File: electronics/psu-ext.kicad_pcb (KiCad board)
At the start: 4 copper layers, 100 x 50 mm, 115 parts, among them J1 TYPE-C-31-M-12, J2 Conn_01x03, J4 Conn_02x02_Odd_Even, K1 HF49FD_005-1H12T, Q1 MMBT2222A, SW1 SW_Push, SW2 SW_Push, U1 USBLC6-2SC6, U2 AP22818AKEWT, U3 LD1117S33, U4 LD1117S33, U5 ESP32-S3-WROOM-1, U6 ISO1540, U7 ADS1115IDGS, U8 INA240A2D, U9 W25Q16JVSS, Y1 FC-135_32.7680KA-A0

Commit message: Add current-sense amplifier offset and fix first-boot download mode
Improve measurement accuracy near zero and enable bidirectional current sensing by adding the current-sense amplifier offset.

Resolve the download-mode issue encountered on first boot.

Signed-off-by: Maxim Pavlov <max.eelabs@gmail.com>
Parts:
- added C24: 100nF, Capacitor_SMD:C_0805_2012Metric, B.Cu at (154.7, 106.6)
- added R27: 22k, Resistor_SMD:R_0805_2012Metric, B.Cu at (157.1, 102.5)
- added R28: 2k, Resistor_SMD:R_0805_2012Metric, B.Cu at (159.1, 102.5)
- added U10: LM321, Package_TO_SOT_SMD:SOT-23-5, B.Cu at (158.0, 106.6)
- moved TP7 0.90 mm to (153.0, 122.1)
- moved TP6 0.85 mm to (157.0, 102.0), turned to 45 degrees
- renumbered C24 to C25, C25 to C26, C26 to C27, C27 to C28, C28 to C29, C29 to C30, C30 to C31, R27 to R29, R28 to R30, R29 to R31, R30 to R32, R31 to R33, R32 to R34, R33 to R35, R34 to R36, R35 to R37, R36 to R38, R37 to R39, R38 to R40, R39 to R41, R40 to R42, R41 to R43, R42 to R44
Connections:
- U8 pad 7: GNDS -> Net-(U10--)
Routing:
- net Net-(U10--): track 0.00 -> 9.25 mm, vias 0 -> 1
- net V3.3-F: track 31.6 -> 36.7 mm
- net Net-(U10-+): track 0.00 -> 4.22 mm
- net GNDS: track 9.90 -> 12.0 mm, vias 27 -> 33
- net /FrontEnd/ALRT: track 9.29 -> 8.77 mm

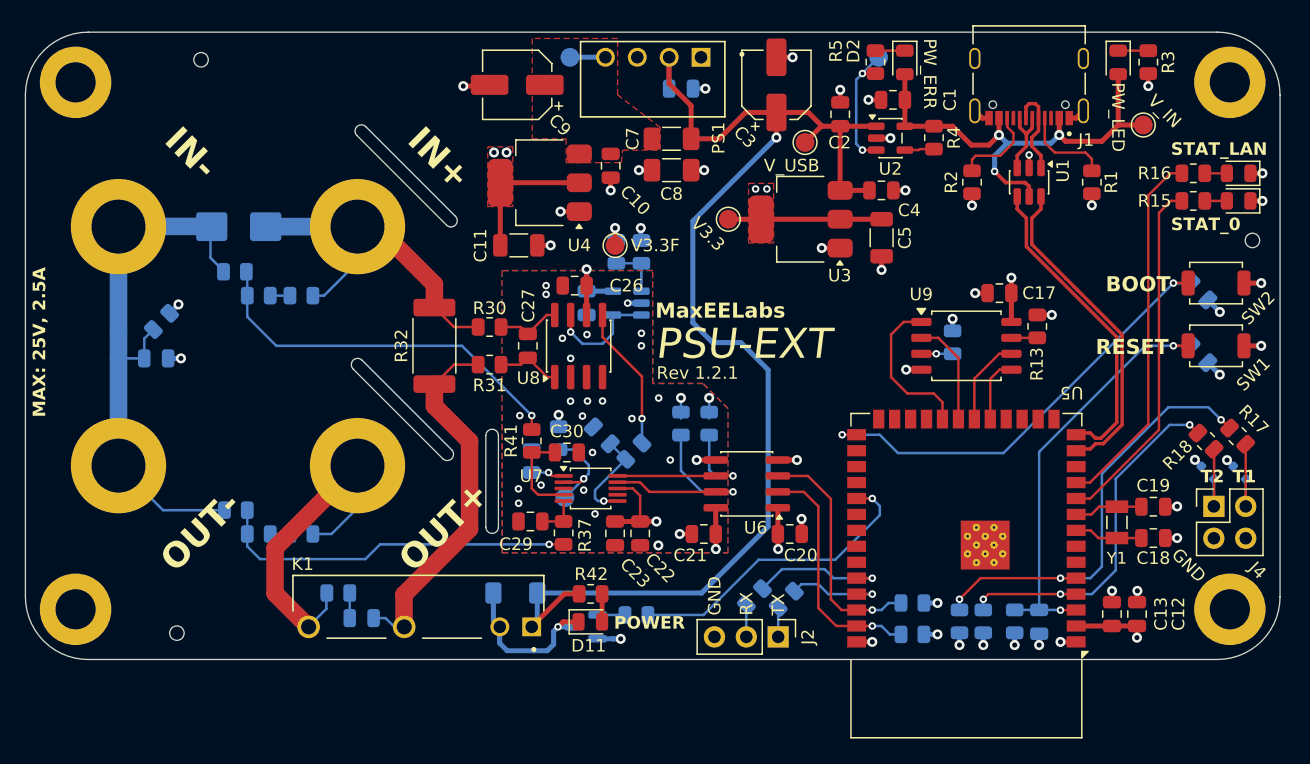
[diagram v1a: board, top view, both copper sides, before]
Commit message: Added input buffernig and negative rail for near-zero measurments
Added I2C_NUM_1 on IO6 (SDA) and IO7 (SCL).

Signed-off-by: Maxim Pavlov <max.eelabs@gmail.com>
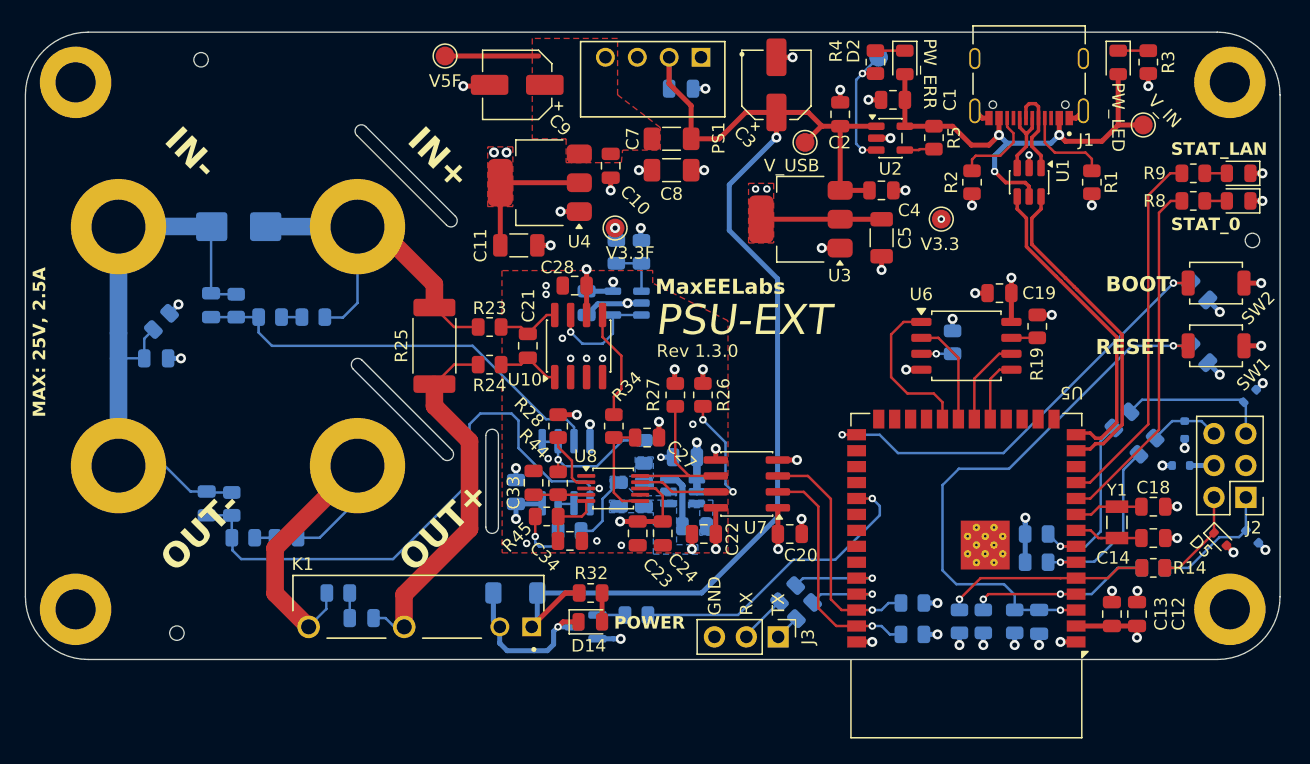
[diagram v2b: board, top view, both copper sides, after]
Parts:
- removed the C25 at (155.9, 117.1)
- removed the C29 at (150.3, 124.0)
- removed J4: Conn_02x02_Odd_Even, Connector_PinHeader_2.54mm:PinHeader_2x02_P2.54mm_Vertical
- removed the R25 at (152.5, 117.4)
- removed the R26 at (150.4, 119.2)
- removed the R29 at (158.5, 118.4)
- removed the R35 at (128.6, 125.0)
- removed TP7: ALRT, TestPoint:TestPoint_Pad_D1.5mm
- added C27: 100nF, Capacitor_SMD:C_0805_2012Metric, F.Cu at (159.6, 117.3)
- added C31: 10nF, Capacitor_SMD:C_0805_2012Metric, B.Cu at (124.8, 106.8)
- added C32: 100nF, Capacitor_SMD:C_0805_2012Metric, B.Cu at (149.1, 121.7)
- added C33: 100nF, Capacitor_SMD:C_0805_2012Metric, F.Cu at (150.5, 120.9)
- added C34: 100nF, Capacitor_SMD:C_0805_2012Metric, F.Cu at (153.4, 125.5)
- added C35: 22uF, Capacitor_SMD:C_0805_2012Metric, B.Cu at (162.6, 118.9)
- added C36: 10uF, Capacitor_SMD:C_0805_2012Metric, B.Cu at (163.3, 124.4)
- added C37: 22uF, Capacitor_SMD:C_0805_2012Metric, B.Cu at (157.3, 121.8)
- added C38: 22uF, Capacitor_SMD:C_0805_2012Metric, B.Cu at (159.3, 121.8)
- added D7: ESD5Zxx, Diode_SMD:D_SOD-523, B.Cu at (207.6, 114.0)
- added D8: ESD5Zxx, Diode_SMD:D_SOD-523, B.Cu at (202.4, 116.7)
- added D9: ESD5Zxx, Diode_SMD:D_SOD-523, B.Cu at (202.1, 119.5)
- added J2: Conn_02x03_Odd_Even, Connector_PinHeader_2.54mm:PinHeader_2x03_P2.54mm_Vertical, F.Cu at (207.3, 122.1)
- added R12: 4.7k, Resistor_SMD:R_0805_2012Metric, B.Cu at (190.6, 127.2)
- added R13: 4.7k, Resistor_SMD:R_0805_2012Metric, B.Cu at (190.6, 125.0)
- added R16: 22R, Resistor_SMD:R_0805_2012Metric, B.Cu at (197.4, 115.9)
- added R17: 22R, Resistor_SMD:R_0805_2012Metric, B.Cu at (199.4, 118.0)
- added R28: 10k, Resistor_SMD:R_0805_2012Metric, F.Cu at (152.5, 116.4)
- added R42: 20k, Resistor_SMD:R_0805_2012Metric, B.Cu at (159.3, 118.5)
- added R43: 20k, Resistor_SMD:R_0805_2012Metric, B.Cu at (153.4, 124.8)
- added R44: 1k, Resistor_SMD:R_0805_2012Metric, F.Cu at (152.5, 121.0)
- added R45: 1k, Resistor_SMD:R_0805_2012Metric, F.Cu at (151.6, 123.6)
- added U11: TSZ122IYDT, Package_SO:SOIC-8_3.9x4.9mm_P1.27mm, B.Cu at (153.1, 120.1)
- added U12: LM2664M6, Package_TO_SOT_SMD:SOT-23-6, B.Cu at (162.4, 121.6)
- C30: value 1nF -> 10nF; moved to B.Cu
- D5, TP5: moved to F.Cu
- R15: renamed from R18; moved to B.Cu
- R26: renamed from R23; moved to F.Cu
- R27: renamed from R24; moved to F.Cu
- R34: value 160k -> 1.5k; moved to F.Cu
- R36: value 20k -> 160k
- R37: value 1k -> 160k; moved to B.Cu
- R41: value 1k -> 20k; moved to B.Cu
- moved C30 29.0 mm to (124.5, 122.6), turned to 90 degrees
- moved R34 26.3 mm to (156.9, 116.4), turned to 90 degrees
- moved R37 26.3 mm to (132.9, 107.7), turned to 180 degrees
- moved R41 25.9 mm to (126.8, 106.8), turned to -90 degrees
- moved R38 19.8 mm to (127.4, 125.3)
- moved R40 18.5 mm to (126.5, 122.6), turned to -90 degrees
- moved TP4 17.0 mm to (183.0, 99.9)
- moved R14 12.5 mm to (199.9, 127.7), turned to 0 degrees
- moved R15 10.9 mm to (199.9, 127.7), turned to 0 degrees
- moved TP5 9.95 mm to (143.4, 86.9), turned to 180 degrees
- moved D6 6.20 mm to (207.8, 125.2), turned to -45 degrees
- moved D5 5.52 mm to (205.2, 125.4), turned to -45 degrees
- moved R36 4.60 mm to (130.8, 125.3), turned to 180 degrees
- moved R27 3.54 mm to (161.8, 113.9)
- moved R26 2.88 mm to (164.0, 113.9)
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- renumbered C18 to C14, C14 to C15, C15 to C16, C16 to C17, C19 to C18, C17 to C19, C27 to C21, C21 to C22, C22 to C24, C28 to C25, C24 to C26, C26 to C28, C31 to C29, D10 to D13, D11 to D14, D12 to D15, H5 to H1, H4 to H10, H3 to H11, H6 to H2, H7 to H3, H8 to H4, H9 to H5, H10 to H6, H11 to H7, H2 to H8, H1 to H9, J2 to J3, R8 to R10, R9 to R11, R17 to R14, R10 to R18, R13 to R19, R14 to R20, R11 to R21, R12 to R22, R30 to R23, R31 to R24, R32 to R25, R33 to R29, R27 to R30, R28 to R31, R42 to R32, R43 to R33, R44 to R35, R5 to R4, R4 to R5, R15 to R8, R16 to R9, U8 to U10, U9 to U6, U6 to U7, U7 to U8, U10 to U9
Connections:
- net /FrontEnd/SCLS renamed /FrontEnd ADC/SCLS
- net /FrontEnd/SDAS renamed /FrontEnd ADC/SDAS
- net /FrontEnd/SENSE_N renamed /FrontEnd ADC/SENSE_N
- net /FrontEnd/SENSE_P renamed /FrontEnd ADC/SENSE_P
- net /FrontEnd/SNT_N renamed /FrontEnd ADC/SNT_N
- C25 pad 1: /FrontEnd/PGND -> PGND
- C30 pad 1: /FrontEnd/AIN0 -> Net-(U11B-+)
- C30 pad 2: GNDS -> PGND
- D13 pad 1: /FrontEnd/PSU_P -> PSU_P
- D13 pad 2: /FrontEnd/PGND -> PGND
- H10 pad 1: /FrontEnd/PGND -> PGND
- H11 pad 1: /FrontEnd/PGND -> PGND
- H8 pad 1: /FrontEnd/PSU_P -> PSU_P
- H9 pad 1: /FrontEnd/LOAD_P -> LOAD_P
- K1 pad 4: /FrontEnd/LOAD_P -> LOAD_P
- R23 pad 2: /FrontEnd/PSU_P -> PSU_P
- R25 pad 2: /FrontEnd/PSU_P -> PSU_P
- R29 pad 1: /FrontEnd/PGND -> PGND
- R34 pad 1: /FrontEnd/LOAD_P -> /FrontEnd ADC/AIN2
- R35 pad 1: /FrontEnd/LOAD_P -> LOAD_P
- R36 pad 1: /FrontEnd/PGND -> LOAD_P
- R36 pad 2: Net-(R35-Pad2) -> Net-(R36-Pad2)
- R37 pad 1: /FrontEnd/AIN1 -> PSU_P
- R37 pad 2: Net-(R35-Pad2) -> Net-(R37-Pad2)
- R38 pad 1: /FrontEnd/PSU_P -> Net-(R36-Pad2)
- R38 pad 2: Net-(R38-Pad2) -> Net-(U11B-+)
- R39 pad 1: Net-(R38-Pad2) -> Net-(R37-Pad2)
- R39 pad 2: Net-(R39-Pad2) -> Net-(U11A-+)
- R40 pad 1: /FrontEnd/PGND -> PGND
- R40 pad 2: Net-(R39-Pad2) -> Net-(U11B-+)
- R41 pad 1: /FrontEnd/AIN0 -> PGND
- R41 pad 2: Net-(R39-Pad2) -> Net-(U11A-+)
- U10 pad 5: Net-(R29-Pad2) -> Net-(R34-Pad2)
- U5 pad 6: unconnected-(U5-IO6-Pad6) -> /ESP32/SDA1
- U5 pad 7: unconnected-(U5-IO7-Pad7) -> /ESP32/SCL1
- U8 pad 1: Net-(U7-ADDR) -> GNDS
- U8 pad 2: /FrontEnd/ALRT -> Net-(U8-ALERT/RDY)
- U8 pad 4: /FrontEnd/AIN0 -> AIN0
- U8 pad 5: /FrontEnd/AIN1 -> AIN1
- U8 pad 6: /FrontEnd/AIN2 -> /FrontEnd ADC/AIN2
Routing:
- net PGND: track 0.00 -> 48.9 mm
- net Net-(U11B-+): track 0.00 -> 46.1 mm
- net /FrontEnd/PGND: track 45.5 -> 0.00 mm
- net LOAD_P: track 0.00 -> 35.7 mm
- net Net-(U11A-+): track 0.00 -> 34.4 mm
- net /FrontEnd/LOAD_P: track 31.3 -> 0.00 mm
- net Net-(R39-Pad2): track 30.6 -> 0.00 mm, vias 1 -> 0
- net PSU_P: track 0.00 -> 30.1 mm
- net Net-(R35-Pad2): track 29.0 -> 0.00 mm, vias 1 -> 0
- net /FrontEnd/PSU_P: track 29.0 -> 0.00 mm
- net /ESP32/TRG2: track 35.1 -> 16.4 mm, vias 3 -> 1
- net /ESP32/SDA1: track 0.00 -> 15.1 mm, vias 0 -> 1
- net /ESP32/SCL1: track 0.00 -> 15.1 mm, vias 0 -> 1
- net /ESP32/TRG1: track 29.7 -> 15.9 mm, vias 3 -> 2
- net Net-(D7-K): track 0.00 -> 12.1 mm
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- added copper zone on B.Cu, net -3V3
- added copper zone on B.Cu, net Net-(U12-CAP+)
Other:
- board text added: "CERN-OHL-S v2 Source: github.com/PSU-Ext-Org"
- board text removed: "CERN-OHL-S v2 Source: github.com/PSU-Ext-Org/psu-ext"
- board text removed: "T1"
- board text removed: "T2"

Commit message: Added IO3 pullup and negative 3V3 rail testpoint, few other PCB layput improvements.
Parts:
- added R14: 10k, Resistor_SMD:R_0805_2012Metric, F.Cu at (193.9, 112.4)
- added TP7: -3V3, TestPoint:TestPoint_Pad_D1.5mm, F.Cu at (160.0, 112.9)
- C7, C8: value 330p 1kV -> 330p
- D6, D7, D8, D9: value ESD5Zxx -> ESD5Z3.3T1G
- R21: renamed from R20; moved to F.Cu
- R3: value 1k -> 2.2k
- moved R21 4.41 mm to (182.1, 105.7), turned to 0 degrees
- moved R43 2.00 mm to (157.3, 118.5)
- moved R27 1.31 mm to (165.3, 113.8)
- moved R28 1.31 mm to (163.1, 113.8)
- moved R35 1.14 mm to (156.9, 117.5)
- moved C27 0.68 mm to (158.9, 117.5), turned to 90 degrees
- moved R20 0.25 mm to (190.9, 108.4)
- renumbered R14 to R15, R15 to R16, R16 to R17, R17 to R18, R18 to R19, R19 to R20, R21 to R22, R22 to R23, R23 to R24, R24 to R25, R25 to R26, R26 to R27, R27 to R28, R28 to R29, R29 to R30, R30 to R31, R31 to R32, R32 to R33, R33 to R34, R34 to R35, R35 to R36, R36 to R37, R37 to R38, R38 to R39, R39 to R40, R40 to R41, R41 to R42, R42 to R43, R43 to R44, R44 to R45, R45 to R46
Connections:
- U5 pad 15: unconnected-(U5-IO3-Pad15) -> Net-(U5-IO3)
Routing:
- net -3V3: track 5.63 -> 14.3 mm, vias 0 -> 1
- net Net-(U6-~{WP}/IO_{2}): track 2.52 -> 8.68 mm, vias 1 -> 2
- net Net-(U5-IO3): track 0.00 -> 3.91 mm
- net Net-(U11A--): track 11.6 -> 10.4 mm
- net /FrontEnd ADC/AIN2: track 8.47 -> 7.63 mm
- net V3.3: track 35.0 -> 35.7 mm, vias 14 -> 15
- net /FrontEnd ADC/SCLS: track 12.0 -> 12.7 mm

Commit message: Fixex for proect before PCBA. TODO. BOM, CPL, EXPORT
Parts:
- D5: value ESD5Zxx -> ESD5Z3.3T1G
- R3: value 2.2k -> 2k
- R31: value 22k -> 20k
- R4: value 1k -> 2k

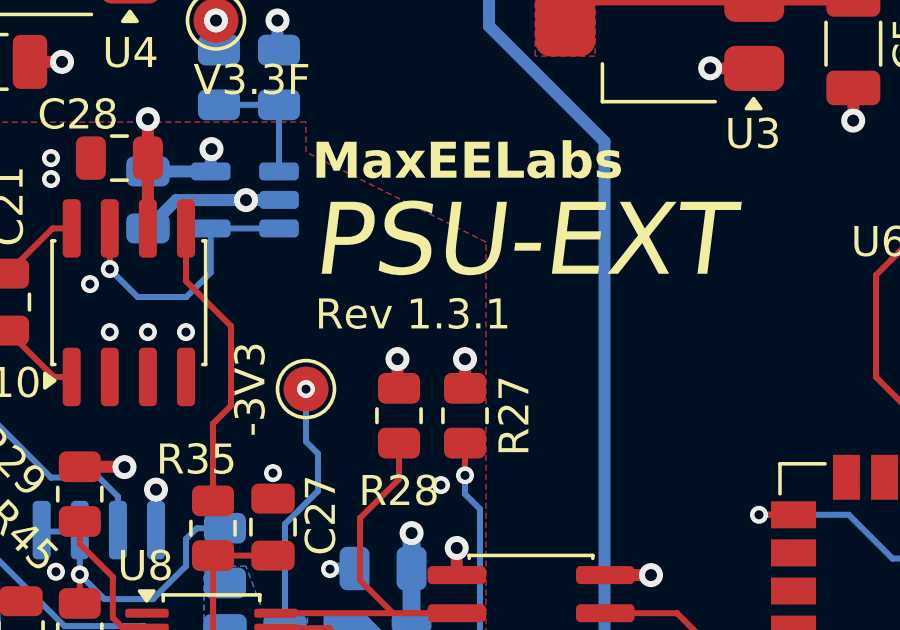
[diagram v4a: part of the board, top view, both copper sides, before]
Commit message: Replaced USB power switch and refreshed manufacturing exports (#5)
Replaced USB power switch U2 with AP2151DWG-7 (0.8 A). Updated schematic and PCB revision metadata and regenerated the BOM, CPL, schematic PDF, and Gerbers.

Updated CHANGES.txt with the design changes and removed completed export TODOs.

Signed-off-by: Maxim Pavlov <max.eelabs@gmail.com>
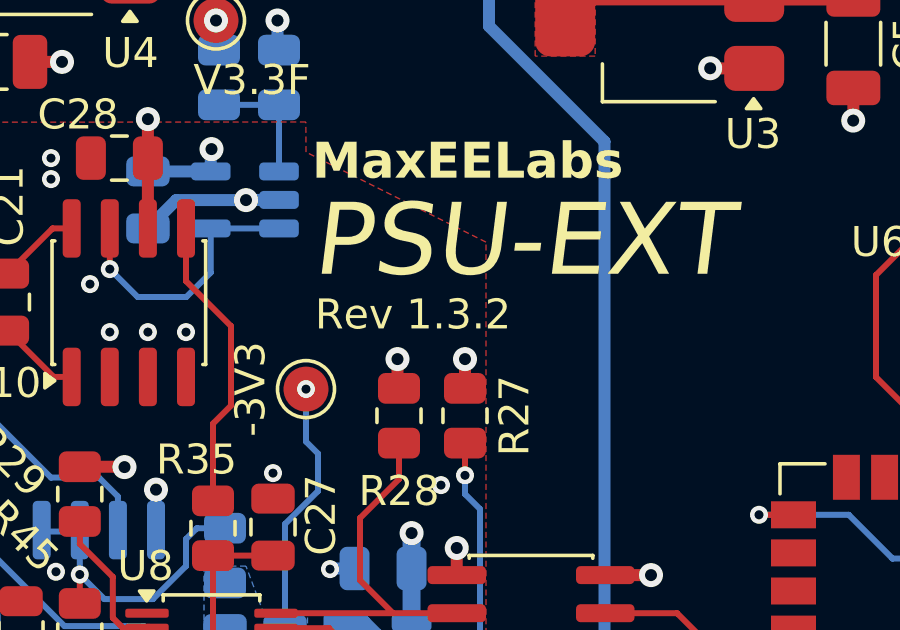
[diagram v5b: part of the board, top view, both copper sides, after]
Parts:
- U2: value AP22818AKEWT -> AP2151DWG-7
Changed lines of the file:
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@@
 	(title_block
 		(title "PSU-EXT")
-		(date "2026-08-08")
-		(rev "1.3.1")
+		(date "2026-10-29")
+		(rev "1.3.2")
 		(company "MaxEELabs")
 	)
@@
 				(font
 					(size 1.27 1.27)
+					(thickness 0.15)
 				)
 			)
@@
 			)
 		)
-		(property "Value" "AP22818AKEWT"
+		(property "Value" "AP2151DWG-7"
 			(at 0 2.4 0)
 			(layer "F.Fab")
@@
 			)
 		)
-		(property "Datasheet" "https://www.diodes.com/assets/Datasheets/AP22816_17_18.pdf"
+		(property "Datasheet" "https://www.mouser.pl/datasheet/3/175/1/AP2141D_51D.pdf"
 			(at 0 0 0)
 			(layer "F.Fab")
@@
 			)
 		)
-		(property "Description" "Current limited 2.0A power switch, single channel, SOT-23-5"
+		(property "Description" "Current limited 0.8A power switch, single channel, SOT-23-5"
 			(at 0 0 0)
 			(layer "F.Fab")
@@
 			)
 		)
-		(property "LCSC" "C5587934"
+		(property "LCSC" "C264075"
 			(at 0 0 0)
 			(layer "F.SilkS")
@@
 	)
 	(segment
+		(start 156 107.544297)
+		(end 156 109.3)
+		(width 0.2)
+		(layer "F.Cu")
+		(net "Net-(R35-Pad2)")
+	)
+	(segment
+		(start 156.9 114.05)
+		(end 156.9 116.624999)
+		(width 0.2)
+		(layer "F.Cu")
+		(net "Net-(R35-Pad2)")
+	)
+	(segment
+		(start 157.5 110.8)
+		(end 157.5 113.45)
+		(width 0.2)
+		(layer "F.Cu")
+		(net "Net-(R35-Pad2)")
+	)
+	(segment
+		(start 157.5 113.45)
+		(end 156.9 114.05)
+		(width 0.2)
+		(layer "F.Cu")
+		(net "Net-(R35-Pad2)")
+	)
+	(segment
+		(start 156 109.3)
+		(end 157.5 110.8)
+		(width 0.2)
+		(layer "F.Cu")
+		(net "Net-(R35-Pad2)")
+	)
+	(segment
 		(start 153.46 108.86)
 		(end 153.5 108.9)
@@
 	)
 	(segment
+		(start 130.4125 107.7125)
+		(end 132.0375 107.7125)
+		(width 0.2)
+		(layer "B.Cu")
+		(net "Net-(R38-Pad2)")
+	)
+	(segment
 		(start 128.5875 108.9375)
 		(end 128.5875 107.7125)
@@
 	)
 	(segment
-		(start 135.850001 129.699996)
-		(end 135.85 131.699995)
-		(width 0.2)
-		(layer "B.Cu")
-		(net "Net-(C29-Pad1)")
-	)
-	(segment
 		(start 157.1 103.424999)
 		(end 159.1 103.424999)
@@
 	)
 	(segment
+		(start 135.850001 129.699996)
+		(end 135.85 131.699995)
+		(width 0.2)
+		(layer "B.Cu")
+		(net "Net-(C29-Pad1)")
+	)
+	(segment
 		(start 161.244999 120.679999)
 		(end 161.907498 120.679999)
@@
 		(net "Net-(U12-CAP-)")
 	)
-	(segment
-		(start 156 107.544297)
-		(end 156 109.3)
-		(width 0.2)
-		(layer "F.Cu")
-		(net "Net-(R35-Pad2)")
-	)
-	(segment
-		(start 156.9 114.05)
-		(end 156.9 116.624999)
-		(width 0.2)
-		(layer "F.Cu")
-		(net "Net-(R35-Pad2)")
-	)
-	(segment
-		(start 157.5 110.8)
-		(end 157.5 113.45)
-		(width 0.2)
-		(layer "F.Cu")
-		(net "Net-(R35-Pad2)")
-	)
-	(segment
-		(start 157.5 113.45)
-		(end 156.9 114.05)
-		(width 0.2)
-		(layer "F.Cu")
-		(net "Net-(R35-Pad2)")
-	)
-	(segment
-		(start 156 109.3)
-		(end 157.5 110.8)
-		(width 0.2)
-		(layer "F.Cu")
-		(net "Net-(R35-Pad2)")
-	)
-	(segment
-		(start 130.4125 107.7125)
-		(end 132.0375 107.7125)
-		(width 0.2)
-		(layer "B.Cu")
-		(net "Net-(R38-Pad2)")
-	)
 	(zone
